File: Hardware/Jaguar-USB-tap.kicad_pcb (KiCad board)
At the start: 2 copper layers, 70 x 45 mm, 32 parts, among them J1 CONN_01X03, J2 CONN_01X02, J3 CONN_01X02, J4 CONN_01X02, J5 USB_B, J6 DB15_FEMALE_HighDensity, J7 CONN_01X05, SW1 SW_DPST_x2, U1 NCP1117ST33T3G, U2 STM32F070CBT6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

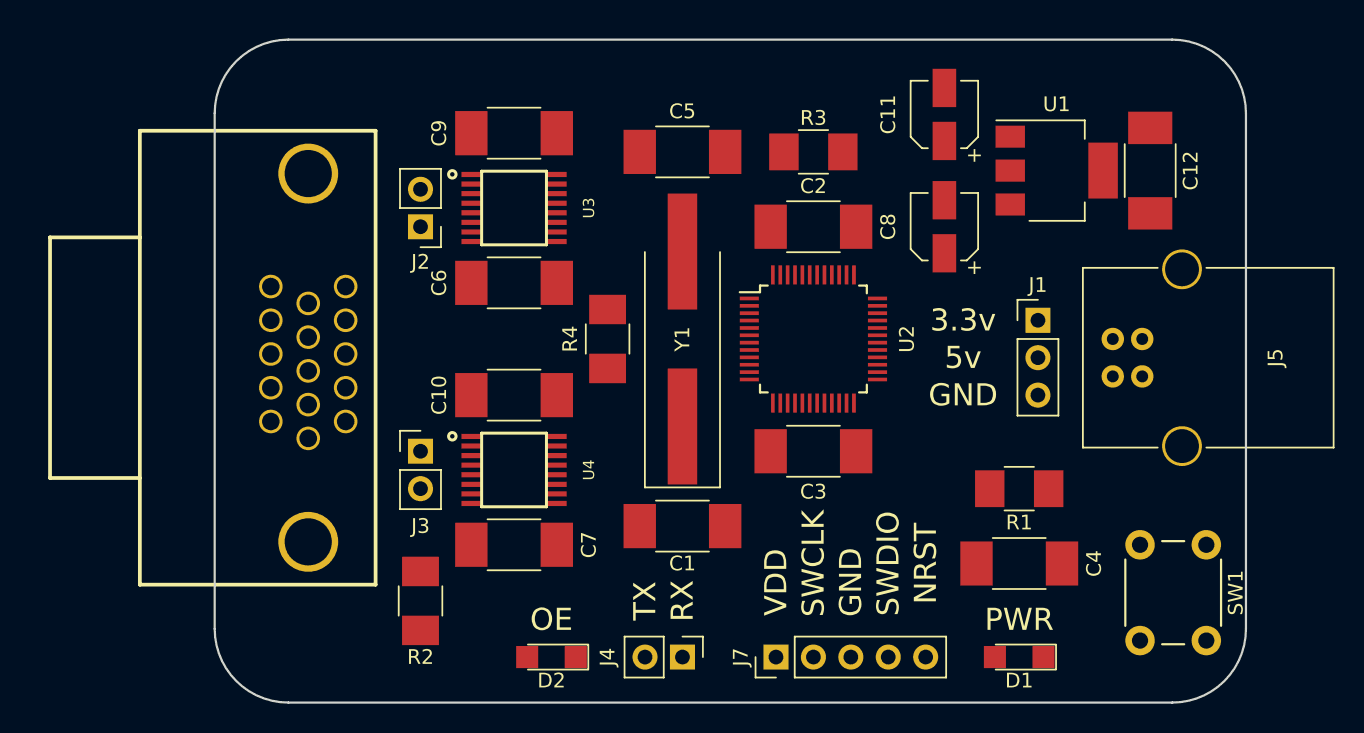
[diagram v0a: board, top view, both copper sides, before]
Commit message: Finish up PCB layout with traces and zone pours.
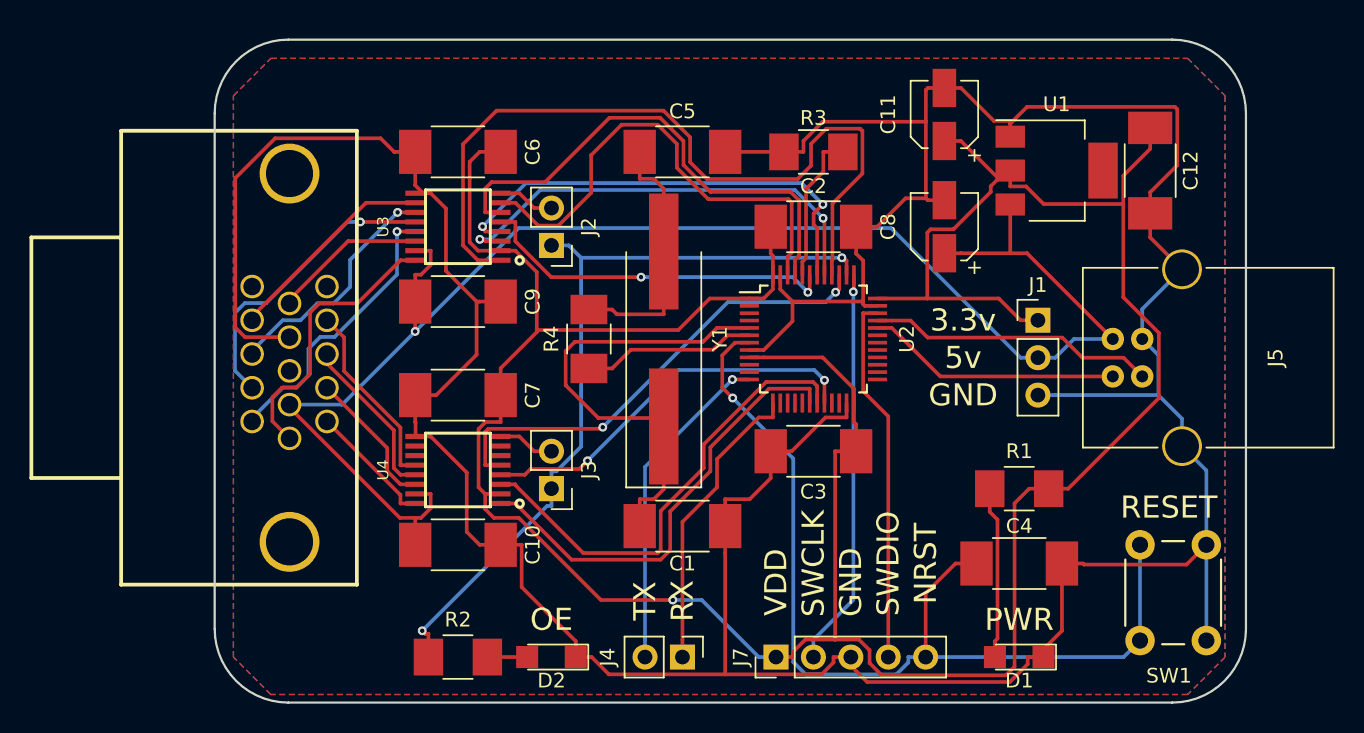
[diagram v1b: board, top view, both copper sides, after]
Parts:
- moved C9 12.0 mm to (16.5, 17.8), turned to 0 degrees
- moved C10 10.9 mm to (16.5, 34.3), turned to 0 degrees
- moved C7 10.9 mm to (16.5, 24.1), turned to 180 degrees
- moved C6 9.67 mm to (16.5, 7.62), turned to 180 degrees
- moved J3 9.25 mm to (22.9, 30.5), turned to 180 degrees
- moved J2 8.98 mm to (22.9, 14.0)
- moved R2 4.58 mm to (16.5, 41.9), turned to 0 degrees
- moved U3 4.02 mm to (16.5, 12.7), turned to 180 degrees
- moved U4 3.81 mm to (16.5, 29.2), turned to 180 degrees
- moved R4 1.27 mm to (25.4, 20.3)
- moved J6 1.27 mm to (5.08, 21.6)
- moved Y1 1.27 mm to (30.5, 20.3)
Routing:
- net GNDREF: track 0.00 -> 268.9 mm
- net VDD: track 0.00 -> 204.6 mm, vias 0 -> 1
- net VCC: track 0.00 -> 106.3 mm, vias 0 -> 1
- net NRST: track 0.00 -> 65.2 mm, vias 0 -> 1
- net R1_VDD: track 0.00 -> 53.8 mm
- net OE: track 0.00 -> 53.7 mm, vias 0 -> 2
- net R5_VDD: track 0.00 -> 34.4 mm
- net R6_VDD: track 0.00 -> 32.9 mm
- net C4_VDD: track 0.00 -> 32.3 mm, vias 0 -> 2
- net C2_VDD: track 0.00 -> 32.0 mm
- net R3_VDD: track 0.00 -> 31.5 mm, vias 0 -> 2
- net Net-(C1-Pad1): track 0.00 -> 31.3 mm
- net C1_VDD: track 0.00 -> 30.9 mm
- net R2_VDD: track 0.00 -> 30.8 mm, vias 0 -> 2
- net SWCLK: track 0.00 -> 27.1 mm, vias 0 -> 1
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- added copper zone on B.Cu, net GNDREF
- added copper zone on F.Cu, net VDD
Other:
- board text added: "RESET"

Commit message: Remove logic-level translation ICs and drive teh controller at 3.3v directly from the uC.
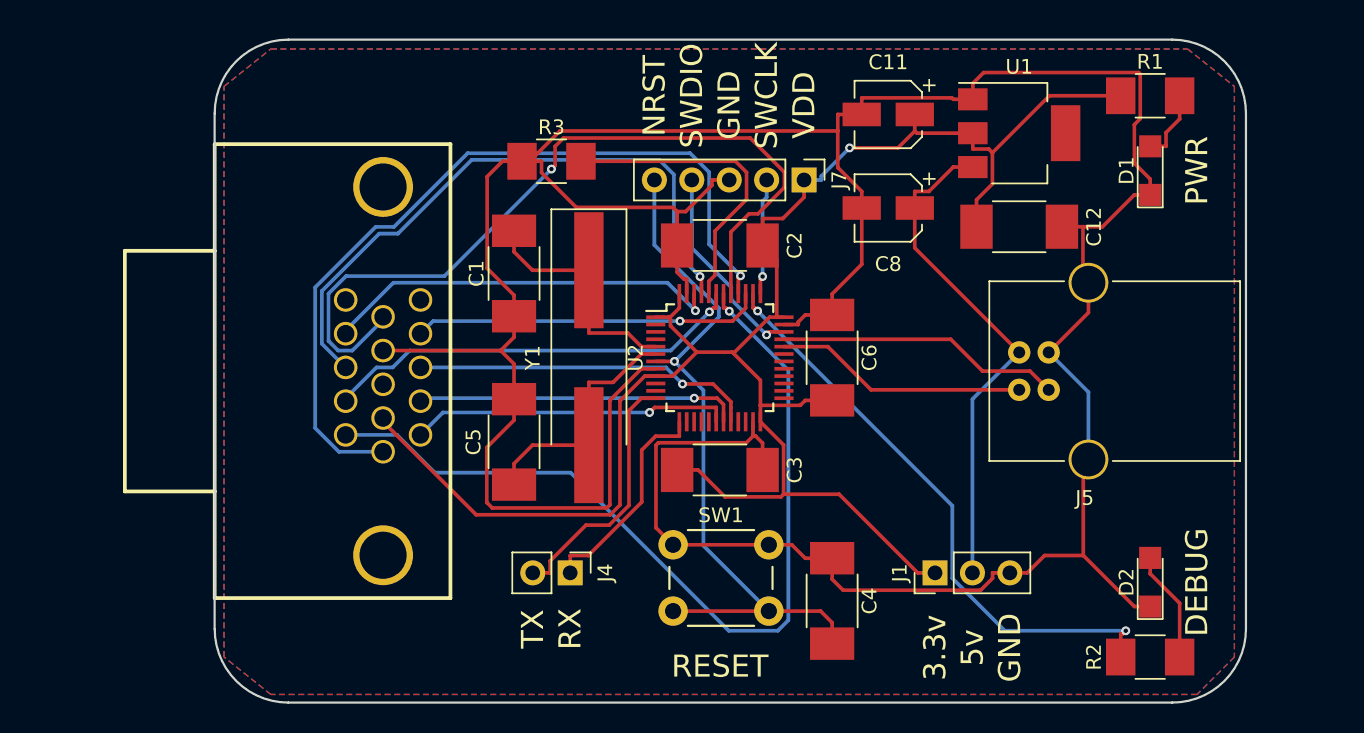
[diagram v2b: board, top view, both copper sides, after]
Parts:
- removed C10, C7, C9: 0.1uF, Capacitors_SMD:C_1812_HandSoldering
- removed the G*** at (35.6, 19.1)
- removed J2, J3: CONN_01X02, Pin_Headers:Pin_Header_Straight_1x02_Pitch2.54mm
- removed R4: 200K, Resistors_SMD:R_1210_HandSoldering
- removed U3, U4: TXB0106, TXB0106:TSSOP16
- added G***: LOGO, SilkArt:Atari-Fuji-2mx2cm, B.Cu at (45.7, 21.6)
- moved R2 47.0 mm to (63.5, 41.9)
- moved D2 41.0 mm to (63.5, 36.8), turned to 90 degrees
- moved SW1 36.2 mm to (31.1, 34.3), turned to 0 degrees
- moved D1 34.2 mm to (63.5, 8.89), turned to 90 degrees
- moved J7 32.4 mm to (40.0, 9.53), turned to 270 degrees
- moved C6 29.0 mm to (41.9, 21.6), turned to 90 degrees
- moved R1 28.1 mm to (63.5, 3.81), turned to 0 degrees
- moved C5 22.8 mm to (20.3, 27.3), turned to 90 degrees
- moved C1 20.6 mm to (20.3, 15.9), turned to 270 degrees
- moved J1 18.5 mm to (48.9, 36.2), turned to 90 degrees
- moved R3 17.8 mm to (22.9, 8.26)
- moved C4 13.0 mm to (41.9, 38.1), turned to 90 degrees
- moved C12 9.67 mm to (54.6, 12.7), turned to 0 degrees
- moved J4 9.52 mm to (24.1, 36.2)
- moved C2 6.48 mm to (34.3, 14.0), turned to 180 degrees
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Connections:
- net OE renamed DEBUG
- net USART_RX renamed UART_RX
- net USART_TX renamed UART_TX
- J6 pad 1: C1_VCC -> C1_VDD
- J6 pad 10: R2_VCC -> R2_VDD
- J6 pad 11: R3_VCC -> R3_VDD
- J6 pad 12: R4_VCC -> R4_VDD
- J6 pad 13: R5_VCC -> R5_VDD
- J6 pad 14: R6_VCC -> R6_VDD
- J6 pad 2: C2_VCC -> C2_VDD
- J6 pad 3: C3_VCC -> C3_VDD
- J6 pad 4: C4_VCC -> C4_VDD
- J6 pad 6: R1_VCC -> R1_VDD
- J6 pad 7: VCC -> VDD
- U2 pad 6: Net-(R4-Pad1) -> Net-(C5-Pad1)
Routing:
- net VDD: track 204.6 -> 126.5 mm
- net VCC: track 106.3 -> 34.8 mm, vias 1 -> 0
- net GNDREF: track 268.9 -> 236.8 mm
- net R3_VDD: track 31.5 -> 59.9 mm, vias 2 -> 1
- net R2_VDD: track 30.8 -> 55.4 mm, vias 2 -> 1
- net R4_VCC: track 20.4 -> 0.00 mm, vias 1 -> 0
- net R3_VCC: track 19.3 -> 0.00 mm, vias 1 -> 0
- net R1_VCC: track 19.3 -> 0.00 mm
- net SWCLK: track 27.1 -> 7.89 mm
- net NRST: track 65.2 -> 48.9 mm
- net R5_VCC: track 16.3 -> 0.00 mm, vias 1 -> 0
- net Net-(C1-Pad1): track 31.3 -> 16.2 mm
- net R6_VCC: track 14.5 -> 0.00 mm
- net DEBUG: track 53.7 -> 40.2 mm
- net C4_VCC: track 12.9 -> 0.00 mm
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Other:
- board text added: "DEBUG"
- board text added: "Jaguar USB Tap Rev 0.3 dgrubb"
- board text removed: "Jaguar USB Tap dgrubb Rev 0.2"
- board text removed: "OE"

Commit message: Remove Atari branding and replace with OSHW logo instead.
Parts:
- G***: footprint SilkArt:Atari-Fuji-2mx2cm -> Symbols:OSHW-Logo_19x20mm_SilkScreen
